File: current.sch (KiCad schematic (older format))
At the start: 28 parts

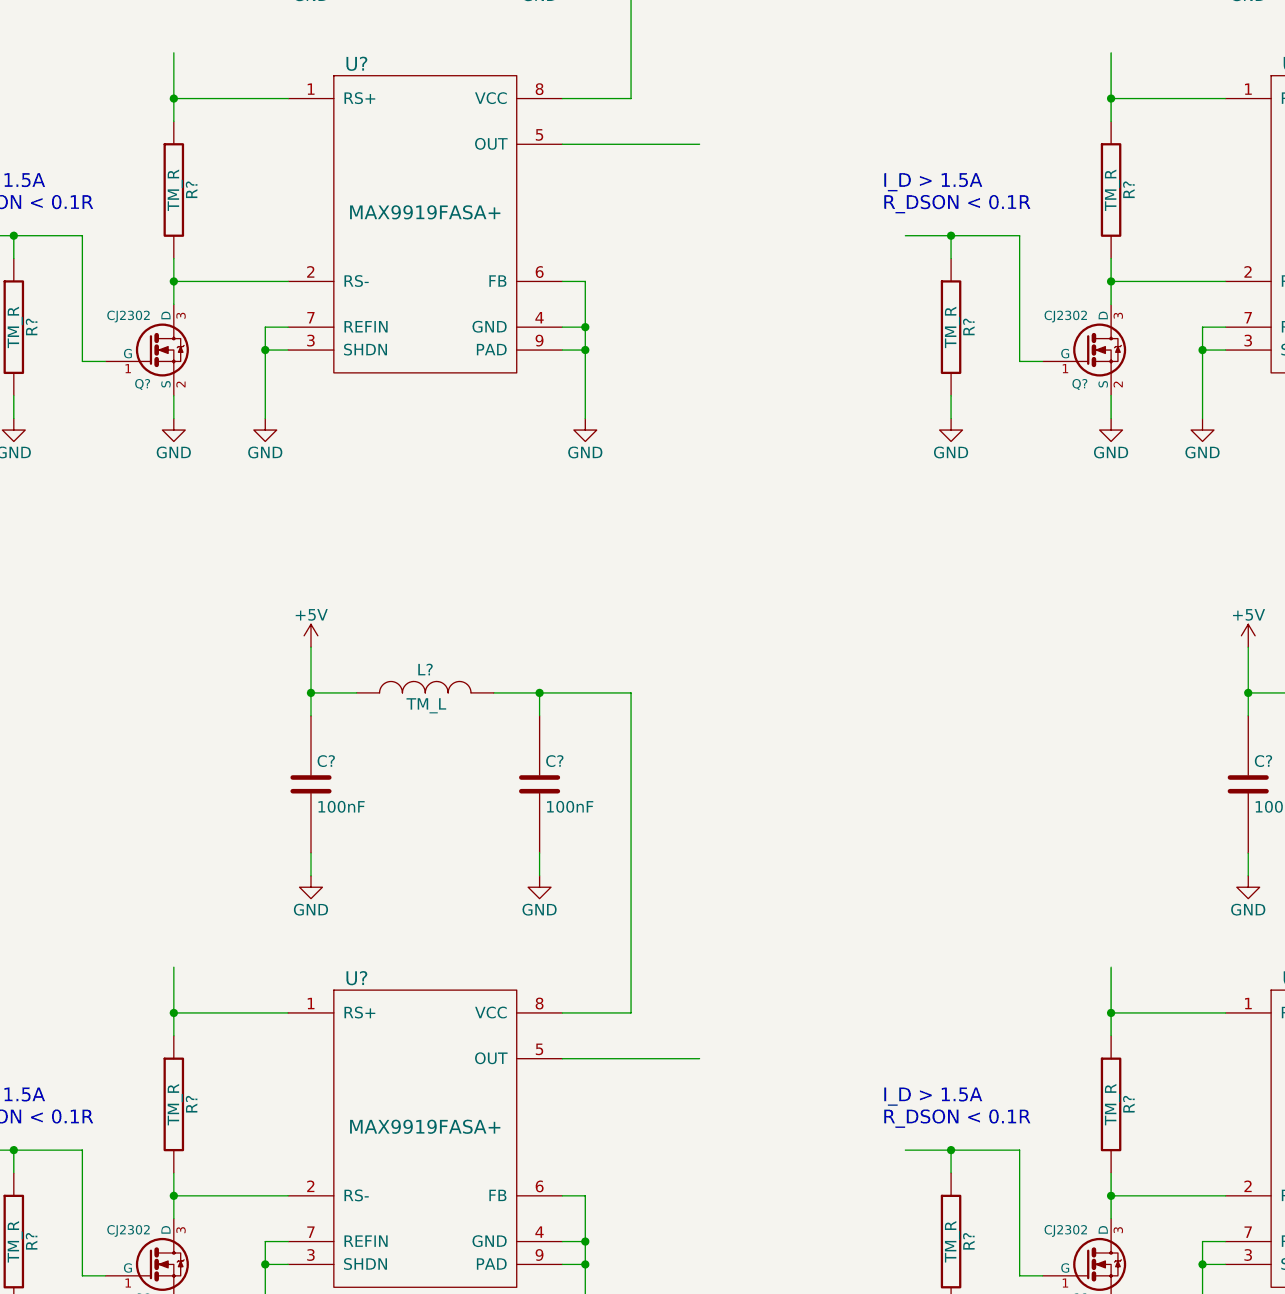
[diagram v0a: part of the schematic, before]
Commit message: ...and now the schematics are in git
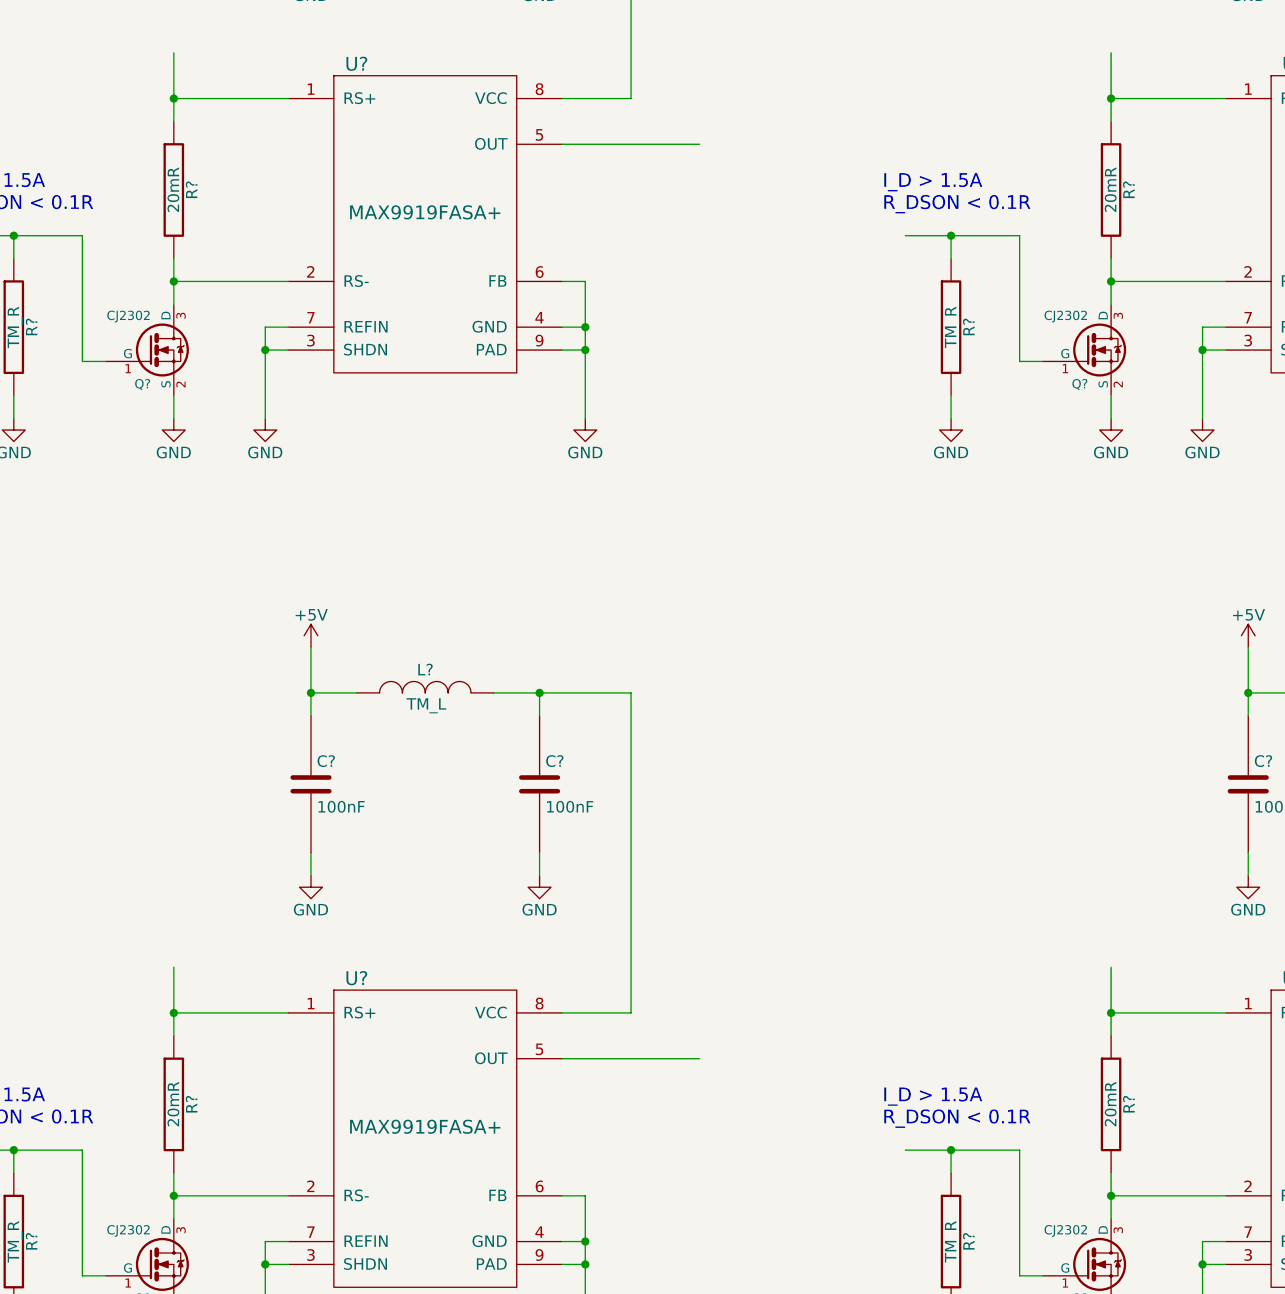
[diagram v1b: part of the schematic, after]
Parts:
- R? (x4): value TM_R -> 20mR
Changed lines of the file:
@@
 P 9200 3600
 F 0 "R?" V 9280 3600 50  0000 C CNN
-F 1 "TM_R" V 9200 3600 50  0000 C CNN
+F 1 "20mR" V 9200 3600 50  0000 C CNN
 F 2 "" V 9130 3600 30  0000 C CNN
 F 3 "" H 9200 3600 30  0000 C CNN
@@
 P 5100 3600
 F 0 "R?" V 5180 3600 50  0000 C CNN
-F 1 "TM_R" V 5100 3600 50  0000 C CNN
+F 1 "20mR" V 5100 3600 50  0000 C CNN
 F 2 "" V 5030 3600 30  0000 C CNN
 F 3 "" H 5100 3600 30  0000 C CNN
@@
 P 5100 7600
 F 0 "R?" V 5180 7600 50  0000 C CNN
-F 1 "TM_R" V 5100 7600 50  0000 C CNN
+F 1 "20mR" V 5100 7600 50  0000 C CNN
 F 2 "" V 5030 7600 30  0000 C CNN
 F 3 "" H 5100 7600 30  0000 C CNN
@@
 P 9200 7600
 F 0 "R?" V 9280 7600 50  0000 C CNN
-F 1 "TM_R" V 9200 7600 50  0000 C CNN
+F 1 "20mR" V 9200 7600 50  0000 C CNN
 F 2 "" V 9130 7600 30  0000 C CNN
 F 3 "" H 9200 7600 30  0000 C CNN

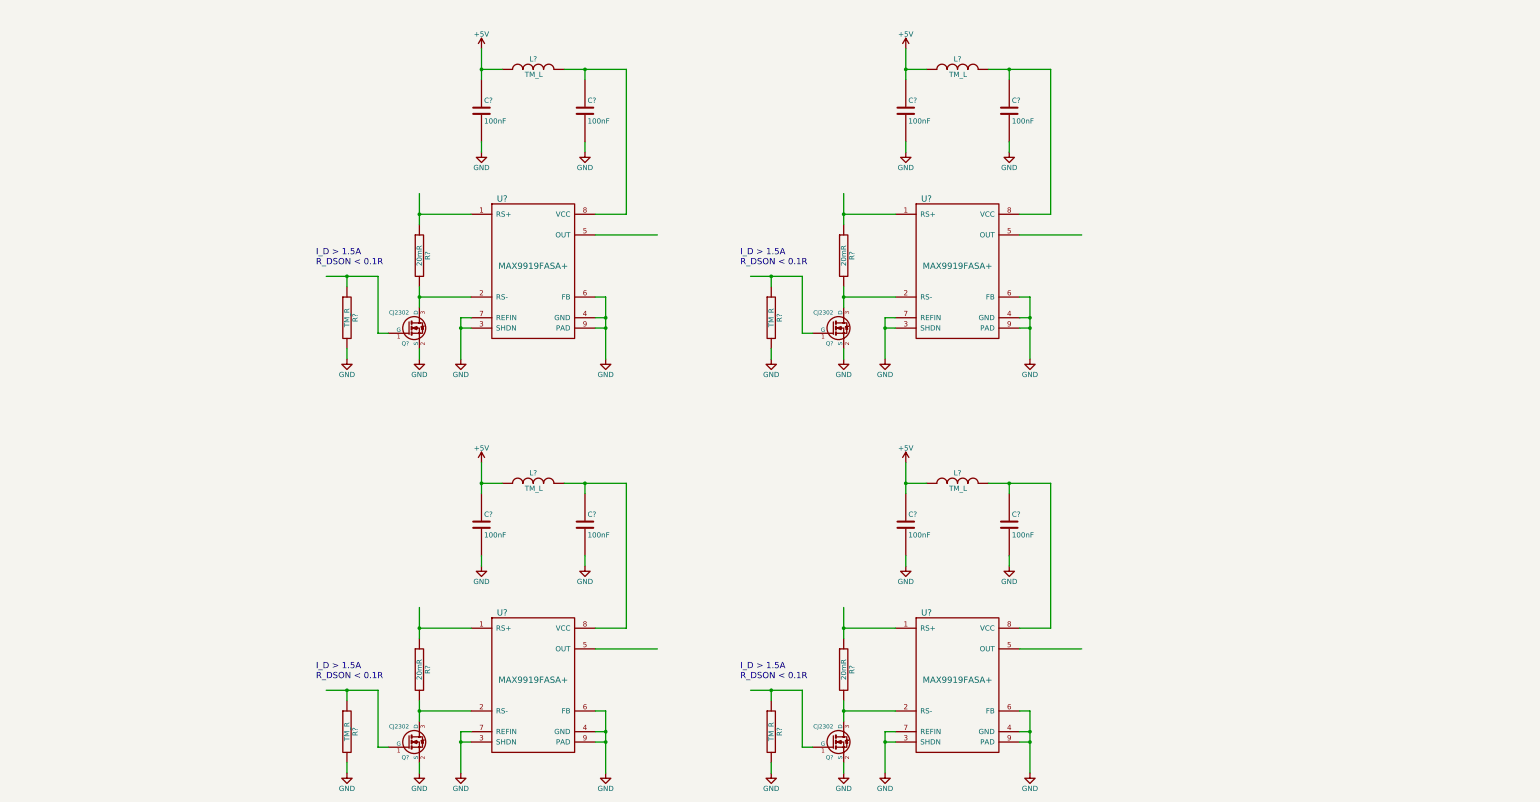
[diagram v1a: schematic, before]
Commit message: pin allocations and finally got the opamp in there
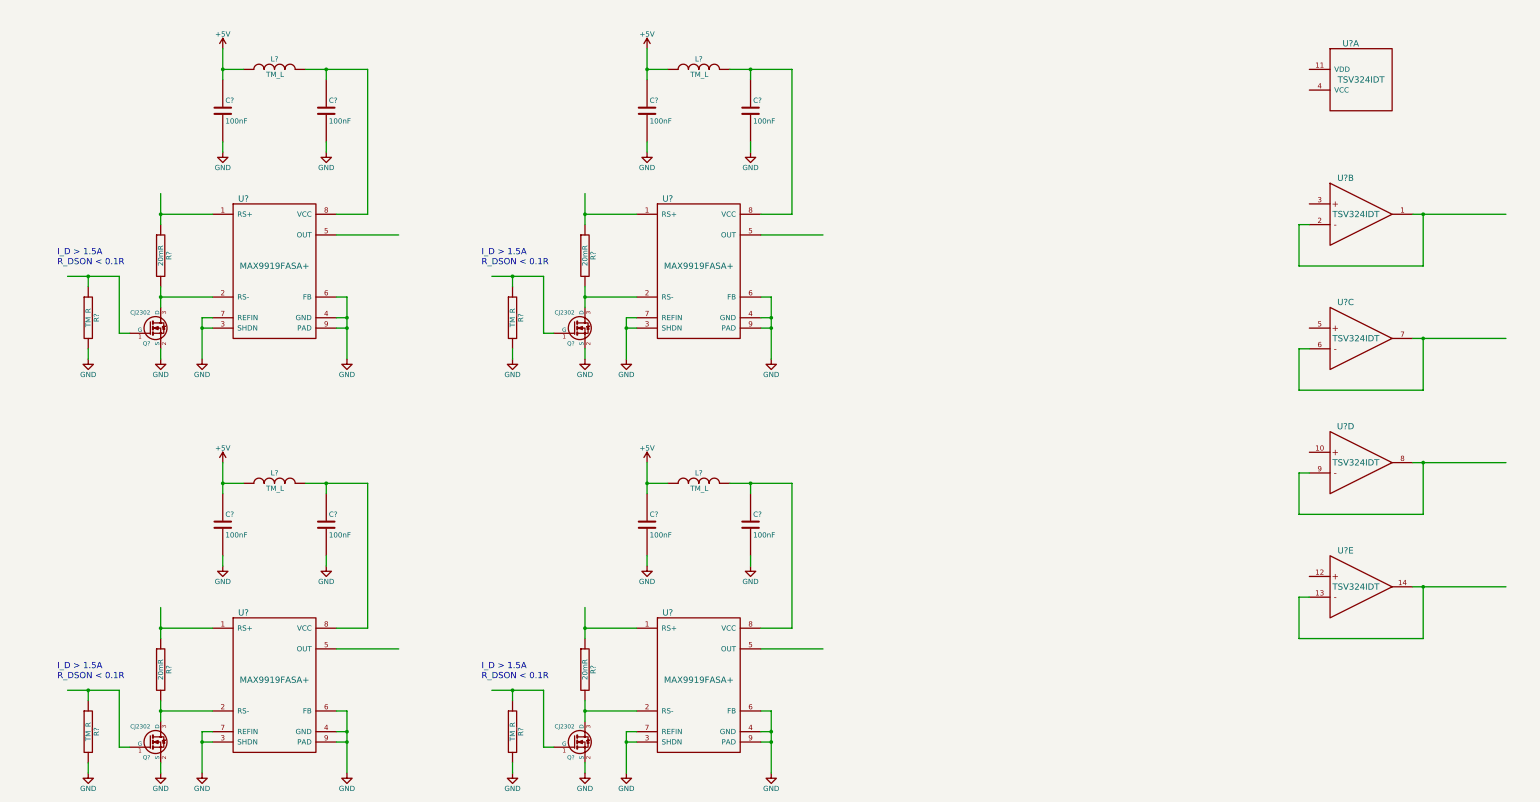
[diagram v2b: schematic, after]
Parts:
- added U? (x5): TSV324IDT, symbol TSV324IDT
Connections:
- wire segments 104 -> 160
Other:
- moved on the sheet: C?, L?, Q?, R?, U?
